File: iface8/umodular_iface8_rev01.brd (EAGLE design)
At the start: 100 x 25 mm, 41 parts, among them U4 SN74HC165DR, U6 SN74HC595D

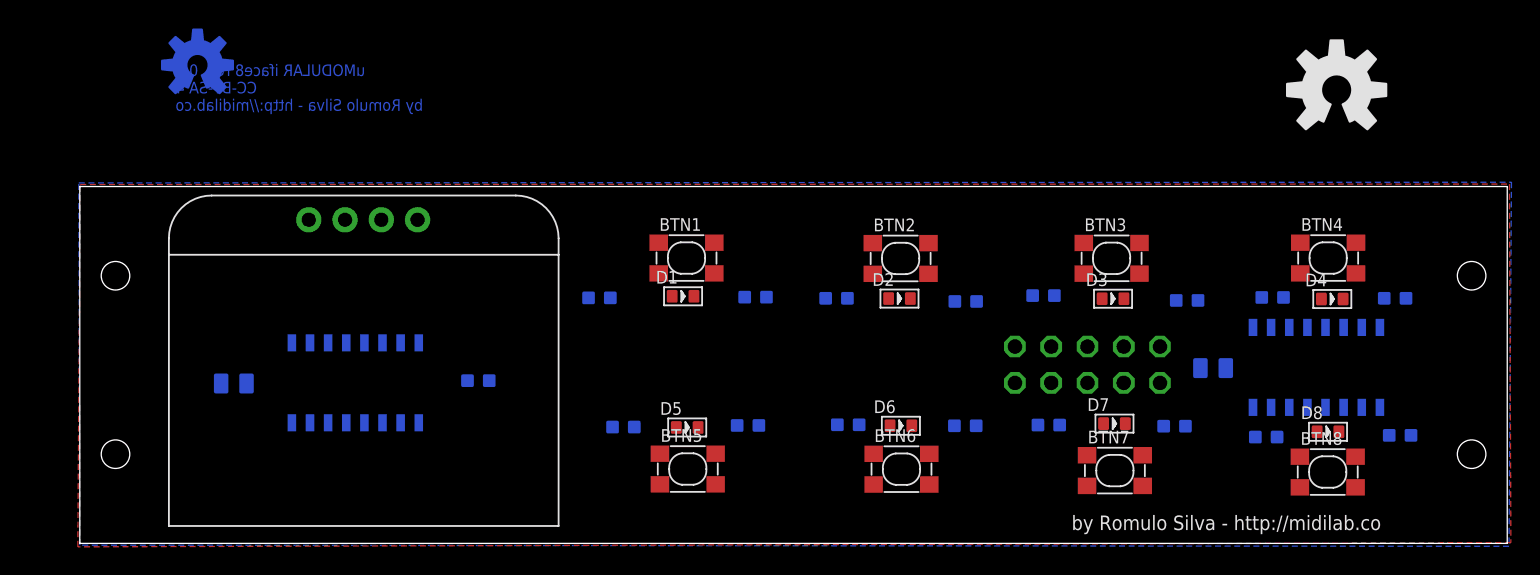
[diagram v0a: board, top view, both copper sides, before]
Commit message: iface8: align components.
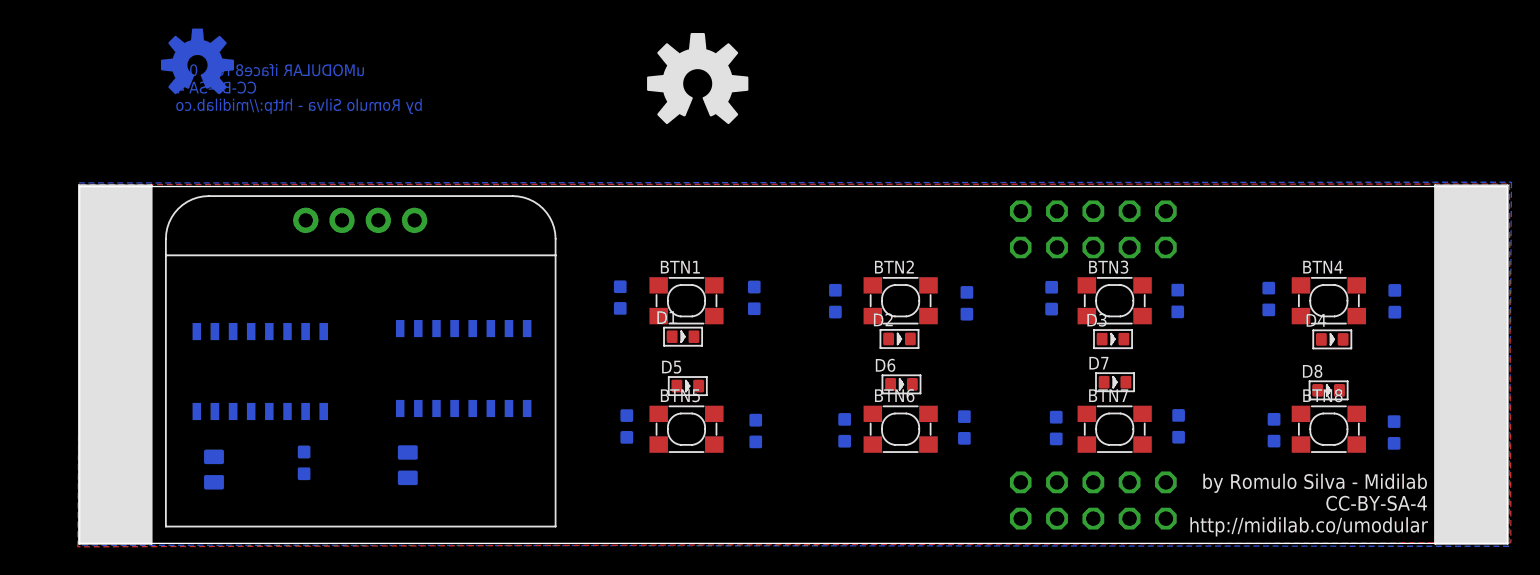
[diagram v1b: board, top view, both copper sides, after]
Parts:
- added CHAIN_OUT: (no value), con-lstb:MA05-2
- added U$2, U$4: (no value), umodular:OLED_0.96_I2C
- moved U6 59.7 mm to (26.9, 12.2)
- moved C6 56.8 mm to (23.0, 5.48), turned to 0 degrees
- moved U$5 44.8 mm to (43.3, 32.2)
- moved R4 13.5 mm to (15.7, 5.64), turned to 0 degrees
- moved DIGITALIO 9.52 mm to (71.0, 3.00)
- moved U4 6.71 mm to (12.6, 12.0)
- moved C5 6.19 mm to (9.40, 5.17), turned to 0 degrees
- moved BTN8 3.00 mm to (87.5, 8.00)
- moved BTN4 2.99 mm to (87.5, 17.0)
- moved BTN1 2.99 mm to (42.5, 17.0)
- moved BTN3 2.98 mm to (72.5, 17.0)
- moved BTN2 2.96 mm to (57.5, 17.0)
- moved D5 2.90 mm to (42.6, 11.0)
- moved D6 2.90 mm to (57.6, 11.1)
- moved D8 2.90 mm to (87.5, 10.7)
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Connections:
- net GND: now also CHAIN_OUT.10
- net I2C_SCL: now also CHAIN_OUT.4
- net I2C_SDA: now also CHAIN_OUT.3
- net SPI_CLOCK: now also CHAIN_OUT.7
- net SPI_CS1: now also CHAIN_OUT.1, DIGITALIO.1; no longer DIGITALIO.2
- net SPI_CS2: now also CHAIN_OUT.2, DIGITALIO.2; no longer DIGITALIO.1
- net SPI_MISO_CHAIN: now also CHAIN_OUT.6
- net SPI_MOSI_CHAIN: now also CHAIN_OUT.8
- net VCC: now also CHAIN_OUT.9
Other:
- board text added: "by Romulo Silva - Midilab CC-BY-SA-4 http://midilab.co/umodular"
- board text removed: "by Romulo Silva - http://midilab.co"

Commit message: iface8: ready to route boy!
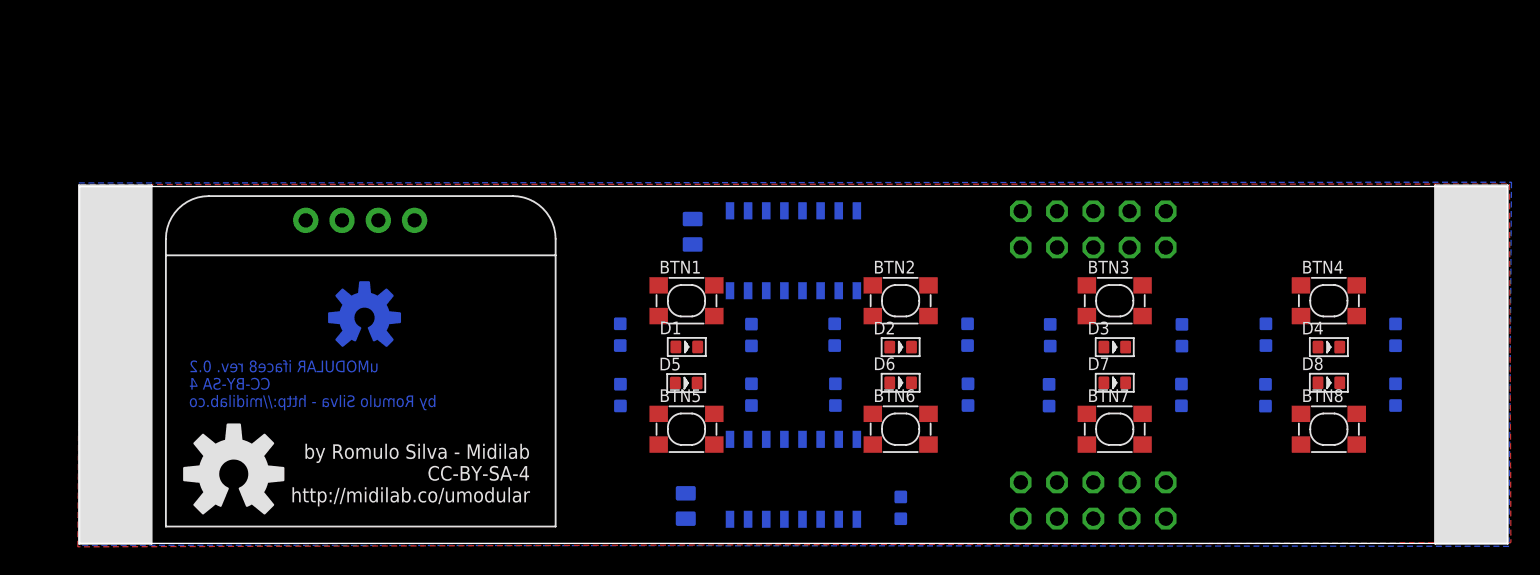
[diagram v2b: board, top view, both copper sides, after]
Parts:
- R10, R11, R12, R4, R5, R6, R7, R8, R9: value 10K 1/10W -> 10K
- moved U$5 42.5 mm to (10.8, 4.86)
- moved R4 41.9 mm to (57.5, 2.49)
- moved U4 38.1 mm to (50.0, 4.49)
- moved C5 33.1 mm to (42.5, 2.62)
- moved C6 25.8 mm to (42.9, 21.8)
- moved U6 24.5 mm to (50.0, 20.5)
- moved U$1 21.2 mm to (19.9, 15.8)
- moved R12 2.65 mm to (92.2, 10.4)
- moved R5 2.61 mm to (47.0, 14.6)
- moved R15 2.60 mm to (68.0, 14.6)
- moved R13 2.60 mm to (37.9, 14.6)
- moved R18 2.58 mm to (52.9, 10.4)
- moved R9 2.57 mm to (47.0, 10.4)
- moved R20 2.52 mm to (83.1, 10.4)
- moved R16 2.51 mm to (83.1, 14.6)
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
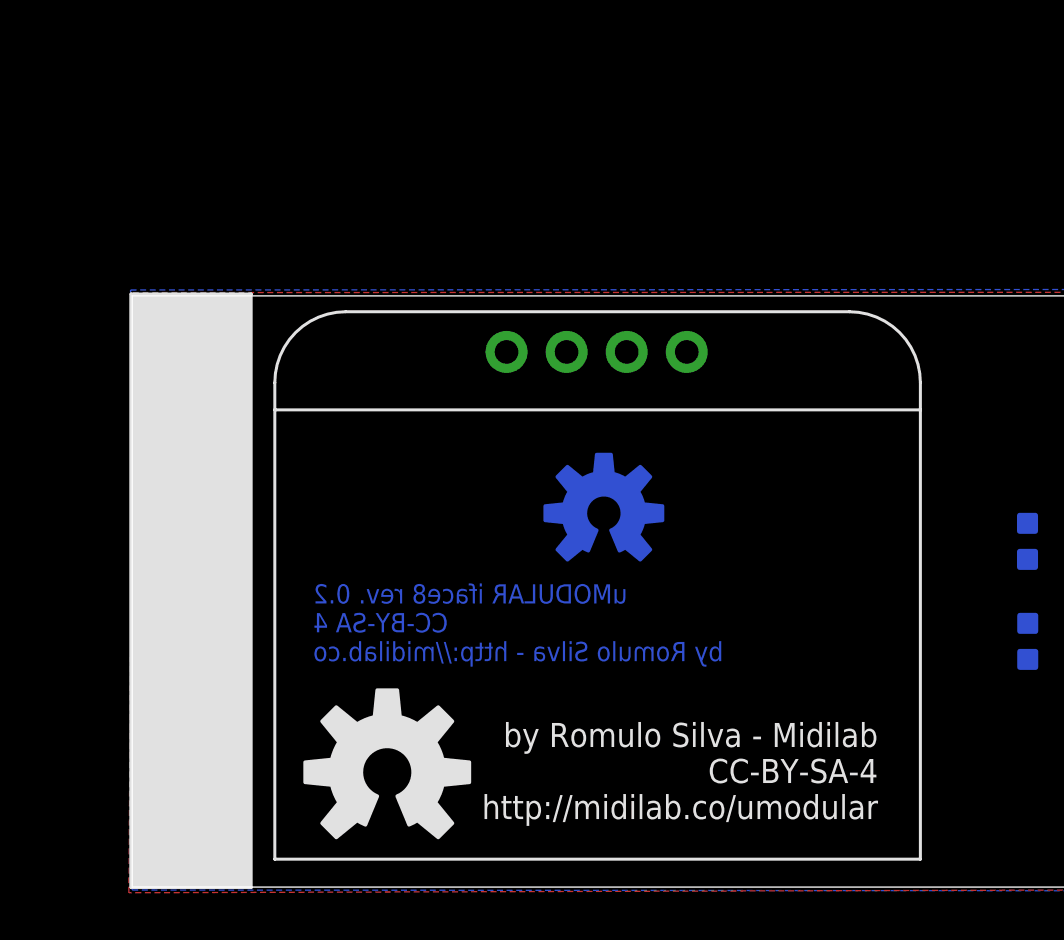
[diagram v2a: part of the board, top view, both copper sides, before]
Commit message: iface8: final oled adjustment
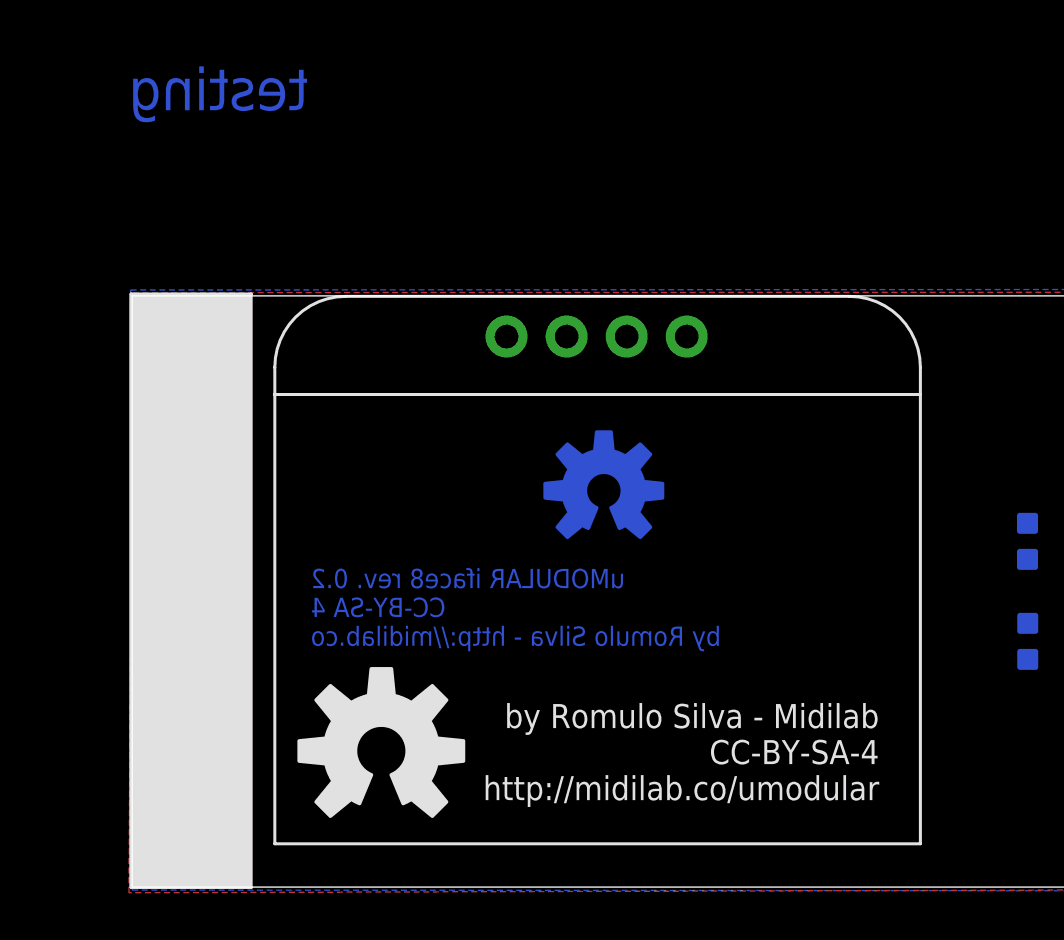
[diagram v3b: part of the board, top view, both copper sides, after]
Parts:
- moved U$1 0.95 mm to (19.9, 16.8)
- moved U$5 0.93 mm to (10.5, 5.75)
- moved U$3 0.65 mm to (20.0, 11.7)
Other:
- board text added: "testing"
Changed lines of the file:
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@@
 <wire x1="99.995" y1="25" x2="0" y2="25" width="0" layer="20"/>
 <wire x1="0" y1="25" x2="0" y2="0" width="0" layer="20"/>
-<text x="7.65" y="12.805" size="0.8128" layer="16" font="vector" rot="MR180">uMODULAR iface8 rev. 0.2
+<text x="7.55" y="13.455" size="0.8128" layer="16" font="vector" rot="MR180">uMODULAR iface8 rev. 0.2
 CC-BY-SA 4
 by Romulo Silva - http://midilab.co</text>
-<text x="31.54" y="6.94" size="1.016" layer="25" rot="R180">by Romulo Silva - Midilab
+<text x="31.59" y="7.74" size="1.016" layer="25" rot="R180">by Romulo Silva - Midilab
 CC-BY-SA-4
- http://midilab.co/umodular</text>
+http://midilab.co/umodular</text>
 <text x="37.37" y="20.52" size="3.81" layer="25">&gt;iface8</text>
+<text x="7.45" y="32.85" size="1.778" layer="16" rot="MR0">testing</text>
 </plain>
 <attributes>
@@
 <attribute name="VALUE" x="71" y="7.196" size="1.27" layer="28" ratio="10" rot="MR180"/>
 </element>
-<element name="U$5" library="SparkFun-Aesthetics" package="OSHW-LOGO-L" value="" x="10.785" y="4.855"/>
-<element name="U$1" library="SparkFun-Aesthetics3" package="OSHW-LOGO-M" value="" x="19.945" y="15.81" smashed="yes"/>
+<element name="U$5" library="SparkFun-Aesthetics" package="OSHW-LOGO-L" value="" x="10.535" y="5.755"/>
+<element name="U$1" library="SparkFun-Aesthetics3" package="OSHW-LOGO-M" value="" x="19.945" y="16.76" smashed="yes"/>
 <element name="BTN6" library="Seeed-Switch-2016" package="SW4-SMD-4.2X3.2X2.5MM" value="DHT-4235A" x="57.5" y="8">
 <attribute name="MPN" value="DHT-4235A" x="57.5" y="8" size="1.778" layer="27" display="off"/>
@@
 <attribute name="PROD_ID" value="IC-11325" x="49.99" y="4.49" size="1.778" layer="28" rot="MR180" display="off"/>
 </element>
-<element name="U$3" library="tft_1.8_1.44_oled_0.96-mod" package="OLED_0.96_I2C" value="OLED_0.96_I2C" x="20" y="11"/>
+<element name="U$3" library="tft_1.8_1.44_oled_0.96-mod" package="OLED_0.96_I2C" value="OLED_0.96_I2C" x="20" y="11.65"/>
 <element name="U6" library="SparkFun-IC-Logic" package="SO16" value="SN74HC595D" x="49.99" y="20.5" rot="MR180">
 <attribute name="PROD_ID" value="IC-07875" x="49.99" y="20.5" size="1.778" layer="28" rot="MR180" display="off"/>
@@
 <wire x1="46.815" y1="1.69" x2="42.45" y2="3.509" width="0" layer="19" extent="16-16"/>
 <wire x1="42.93" y1="20.941" x2="44.45" y2="15.925" width="0" layer="19" extent="1-16"/>
-<wire x1="18.37" y1="22.63" x2="42.93" y2="20.941" width="0" layer="19" extent="16-16"/>
+<wire x1="18.37" y1="23.28" x2="42.93" y2="20.941" width="0" layer="19" extent="16-16"/>
 </signal>
 <signal name="VCC">
@@
 <wire x1="45.545" y1="1.69" x2="47.05" y2="9.658" width="0" layer="19" extent="16-16"/>
 <wire x1="42.45" y1="1.731" x2="45.545" y2="1.69" width="0" layer="19" extent="16-16"/>
-<wire x1="15.83" y1="22.63" x2="42.93" y2="22.719" width="0" layer="19" extent="16-16"/>
+<wire x1="15.83" y1="23.28" x2="42.93" y2="22.719" width="0" layer="19" extent="16-16"/>
 </signal>
 <signal name="SPI_CLOCK">
@@
 <contactref element="CHAIN_OUT" pad="4"/>
 <wire x1="68.46" y1="1.735" x2="73.54" y2="23.27" width="0" layer="19" extent="1-1"/>
-<wire x1="20.91" y1="22.63" x2="68.46" y2="1.735" width="0" layer="19" extent="1-1"/>
+<wire x1="20.91" y1="23.28" x2="68.46" y2="1.735" width="0" layer="19" extent="1-1"/>
 </signal>
 <signal name="I2C_SDA">
@@
 <contactref element="CHAIN_OUT" pad="3"/>
 <wire x1="68.46" y1="4.275" x2="73.54" y2="20.73" width="0" layer="19" extent="1-1"/>
-<wire x1="23.45" y1="22.63" x2="68.46" y2="4.275" width="0" layer="19" extent="1-1"/>
+<wire x1="23.45" y1="23.28" x2="68.46" y2="4.275" width="0" layer="19" extent="1-1"/>
 </signal>
 </signals>
